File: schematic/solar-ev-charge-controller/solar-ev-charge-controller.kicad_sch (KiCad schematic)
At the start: 26 parts, among them J1 Conn_01x02, K1 SRD-05VDC-SL-C, Q2 IRL744N, Q3 IRL744N, U1 LM393, U2 SFH617A-3, U3 SFH617A-3, U4 SFH617A-3

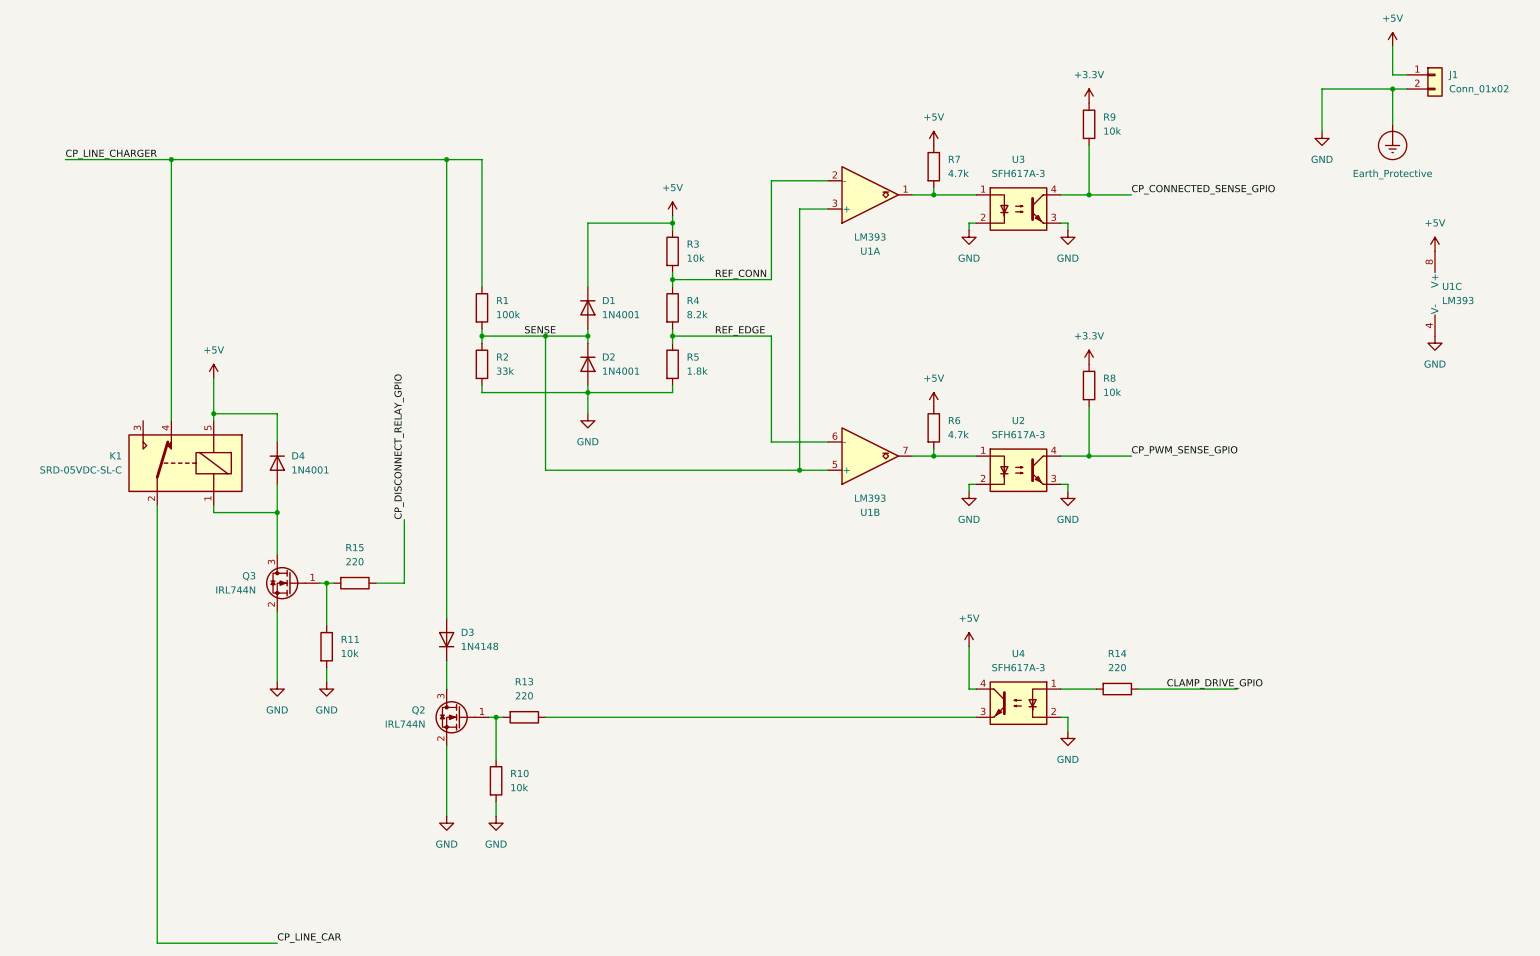
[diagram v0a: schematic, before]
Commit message: Add BLE provisioning, grid source & build tools
Add a BLE NUS-based provisioning server (src/ble_config.cpp, include/ble_config.h) and runtime WiFi/inverter/config plumbing (shared_state RuntimeConfig + setters/getters). Introduce a grid-data abstraction (src/grid_data_source.h) and a DTSU666 implementation (src/grid_source_dtsu666.cpp) that reads power via the Sungrow WiNet-S Modbus TCP interface. Wire solar_control to the new data source, remove the old Modbus helper, and start BLE at boot (main.cpp). Add .env.example and pre-build secret sync + helper scripts (tools/sync_secrets.py, tools/ota_upload.py, tools/sync_env_vars.py) and update platformio.ini to run the pre-build step and use NimBLE. Remove LCD/status display references, update config and docs, and rename/move KiCad schematic files. Device now advertises over BLE until provisioned; WiFi/inverter creds are provisioned via BLE.
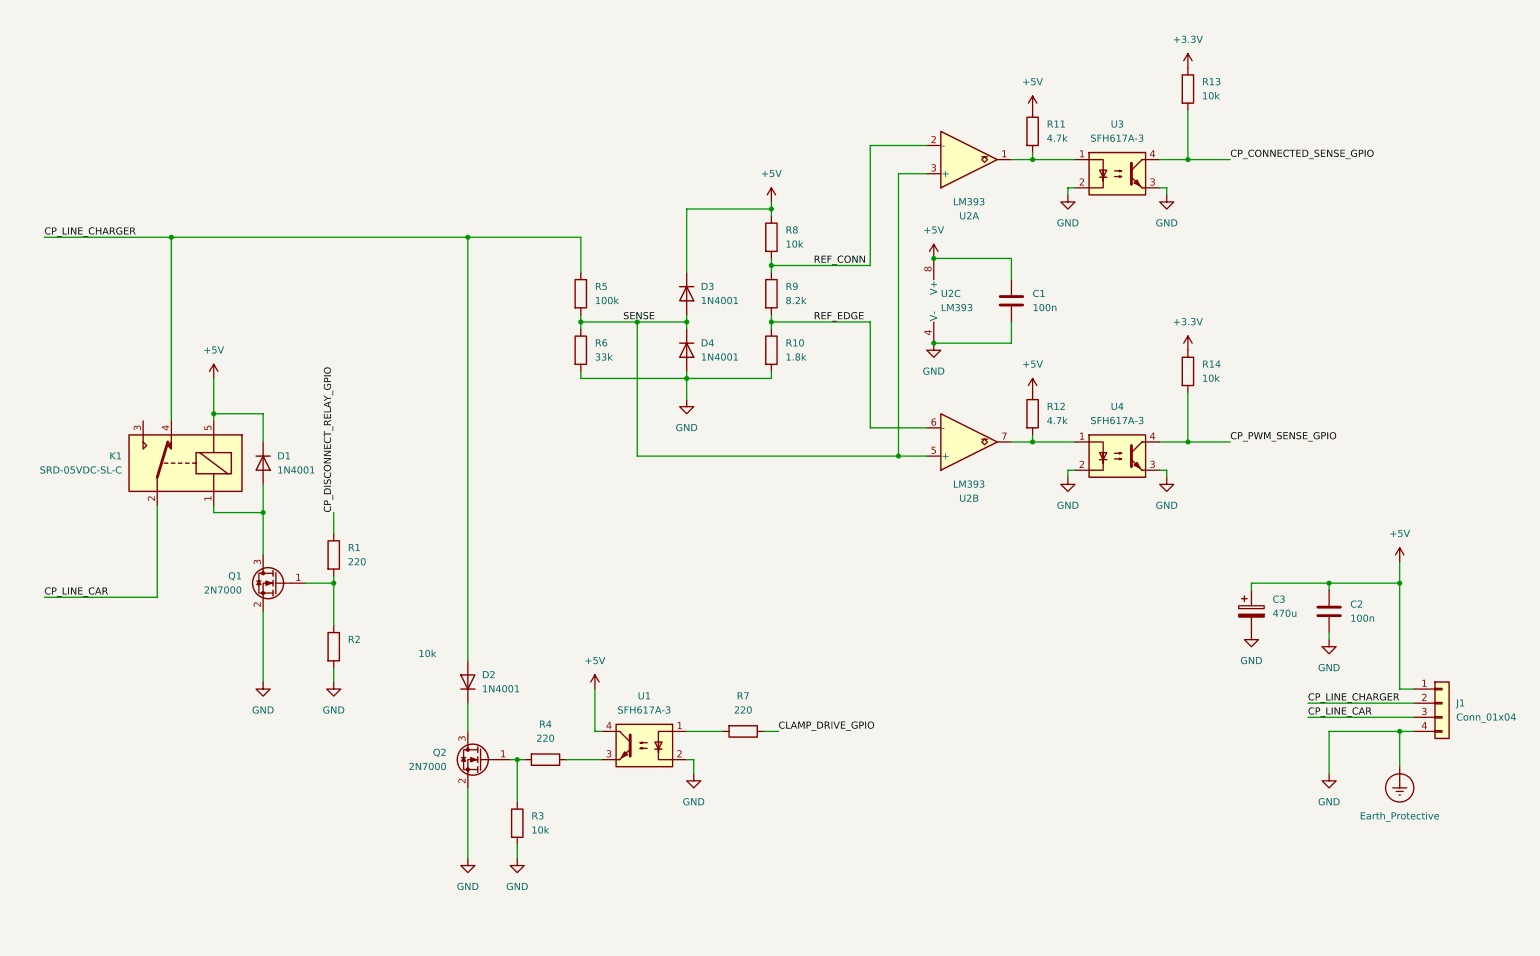
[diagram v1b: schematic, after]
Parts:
- removed D3: 1N4148, Diode_THT:D_DO-35_SOD27_P7.62mm_Horizontal, symbol Diode:1N4148
- removed J1: Conn_01x02, TerminalBlock:TerminalBlock_Xinya_XY308-2.54-2P_1x02_P2.54mm_Horizontal, symbol Connector_Generic:Conn_01x02
- added C1, C2: 100n, symbol Device:C
- added C3: 470u, symbol Device:C_Polarized
- added D2: 1N4001, symbol Device:D
- added J1: Conn_01x04, symbol Connector_Generic:Conn_01x04
- Q1: renamed from Q3; value IRL744N -> 2N7000
- Q2: value IRL744N -> 2N7000
- renumbered D4 to D1, D1 to D3, D2 to D4, R15 to R1, R5 to R10, R7 to R11, R6 to R12, R9 to R13, R8 to R14, R11 to R2, R10 to R3, R13 to R4, R1 to R5, R2 to R6, R14 to R7, R3 to R8, R4 to R9, U4 to U1, U1 to U2, U2 to U4
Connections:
- net +5V: now also C1.1, C2.1, C3.1, J1.1 (Pin_1)
- net CP_LINE_CAR: now also J1.3 (Pin_3)
- net CP_LINE_CHARGER: now also D2.2 (A), J1.2 (Pin_2)
- net Earth_Protective: now also C1.2, C2.2, C3.2, J1.4 (Pin_4)
- net at Q2.3 (D): now also D2.1 (K)
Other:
- title: CCS2 CP Interceptor -> CP Interceptor
- moved on the sheet: D1, D3, D4, Q1, Q2, R1, R10, R11, R12, R13, R14, R2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
